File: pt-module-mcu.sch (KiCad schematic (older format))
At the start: 14 parts, among them SW8 SW_Push, SW9 SW_Push, U8 STM32F334R8Tx

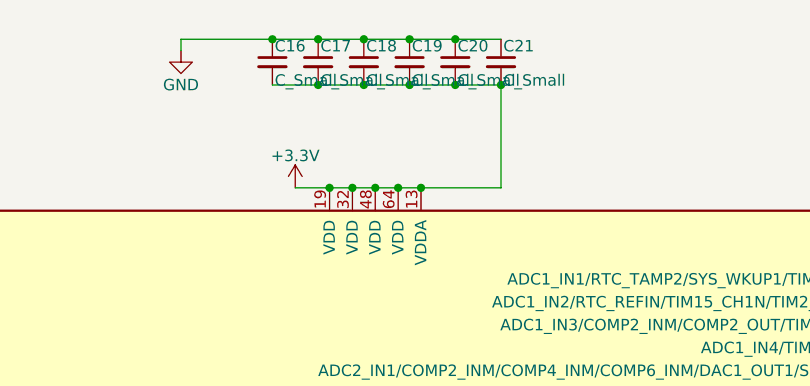
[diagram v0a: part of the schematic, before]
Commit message: Determined MCU power capacitor sizes, at last
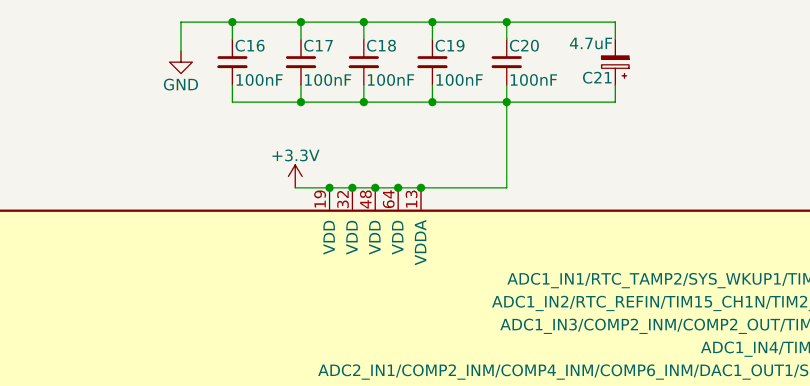
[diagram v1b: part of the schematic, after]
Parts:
- removed C21: C_Small, symbol C_Small
- added C21: 4.7uF, symbol CP_Small
- C16, C17, C18, C19, C20: value C_Small -> 100nF
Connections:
- net +3V3: now also C21.1
- net GND: now also C21.2
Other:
- moved on the sheet: C16, C17, C19, C20
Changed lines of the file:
@@
 $EndComp
 $Comp
-L GND #PWR079
+L GND #PWR74
 U 1 1 597EDE48
 P 1150 6800
-F 0 "#PWR079" H 1150 6550 50  0001 C CNN
+F 0 "#PWR74" H 1150 6550 50  0001 C CNN
 F 1 "GND" H 1150 6650 50  0000 C CNN
 F 2 "" H 1150 6800 50  0001 C CNN
@@
 $EndComp
 $Comp
-L GND #PWR080
+L GND #PWR77
 U 1 1 597EDE64
 P 1850 6800
-F 0 "#PWR080" H 1850 6550 50  0001 C CNN
+F 0 "#PWR77" H 1850 6550 50  0001 C CNN
 F 1 "GND" H 1850 6650 50  0000 C CNN
 F 2 "" H 1850 6800 50  0001 C CNN
@@
 $EndComp
 $Comp
-L GND #PWR081
+L GND #PWR75
 U 1 1 597EF838
 P 1750 1850
-F 0 "#PWR081" H 1750 1600 50  0001 C CNN
+F 0 "#PWR75" H 1750 1600 50  0001 C CNN
 F 1 "GND" H 1750 1700 50  0000 C CNN
 F 2 "" H 1750 1850 50  0001 C CNN
@@
 L C_Small C17
 U 1 1 597F1898
-P 6000 1100
-F 0 "C17" H 6010 1170 50  0000 L CNN
-F 1 "C_Small" H 6010 1020 50  0000 L CNN
-F 2 "" H 6000 1100 50  0001 C CNN
-F 3 "" H 6000 1100 50  0001 C CNN
-	1    6000 1100
-	1    0    0    -1
-$EndComp
-$Comp
-L C_Small C18
-U 1 1 597F1903
-P 6200 1100
-F 0 "C18" H 6210 1170 50  0000 L CNN
-F 1 "C_Small" H 6210 1020 50  0000 L CNN
-F 2 "" H 6200 1100 50  0001 C CNN
-F 3 "" H 6200 1100 50  0001 C CNN
-	1    6200 1100
+P 5925 1100
+F 0 "C17" H 5935 1170 50  0000 L CNN
+F 1 "100nF" H 5935 1020 50  0000 L CNN
+F 2 "" H 5925 1100 50  0001 C CNN
+F 3 "" H 5925 1100 50  0001 C CNN
+	1    5925 1100
 	1    0    0    -1
 $EndComp
@@
 L C_Small C19
 U 1 1 597F1997
-P 6400 1100
-F 0 "C19" H 6410 1170 50  0000 L CNN
-F 1 "C_Small" H 6410 1020 50  0000 L CNN
-F 2 "" H 6400 1100 50  0001 C CNN
-F 3 "" H 6400 1100 50  0001 C CNN
-	1    6400 1100
+P 6500 1100
+F 0 "C19" H 6510 1170 50  0000 L CNN
+F 1 "100nF" H 6510 1020 50  0000 L CNN
+F 2 "" H 6500 1100 50  0001 C CNN
+F 3 "" H 6500 1100 50  0001 C CNN
+	1    6500 1100
 	1    0    0    -1
 $EndComp
@@
 L C_Small C20
 U 1 1 597F19E6
-P 6600 1100
-F 0 "C20" H 6610 1170 50  0000 L CNN
-F 1 "C_Small" H 6610 1020 50  0000 L CNN
-F 2 "" H 6600 1100 50  0001 C CNN
-F 3 "" H 6600 1100 50  0001 C CNN
-	1    6600 1100
+P 6825 1100
+F 0 "C20" H 6835 1170 50  0000 L CNN
+F 1 "100nF" H 6835 1020 50  0000 L CNN
+F 2 "" H 6825 1100 50  0001 C CNN
+F 3 "" H 6825 1100 50  0001 C CNN
+	1    6825 1100
 	1    0    0    -1
 $EndComp
@@
 L C_Small C16
 U 1 1 597F1A58
-P 5800 1100
-F 0 "C16" H 5810 1170 50  0000 L CNN
-F 1 "C_Small" H 5810 1020 50  0000 L CNN
-F 2 "" H 5800 1100 50  0001 C CNN
-F 3 "" H 5800 1100 50  0001 C CNN
-	1    5800 1100
-	1    0    0    -1
-$EndComp
-$Comp
-L C_Small C21
-U 1 1 597F1AA1
-P 6800 1100
-F 0 "C21" H 6810 1170 50  0000 L CNN
-F 1 "C_Small" H 6810 1020 50  0000 L CNN
-F 2 "" H 6800 1100 50  0001 C CNN
-F 3 "" H 6800 1100 50  0001 C CNN
-	1    6800 1100
-	1    0    0    -1
-$EndComp
-$Comp
-L GND #PWR082
+P 5625 1100
+F 0 "C16" H 5635 1170 50  0000 L CNN
+F 1 "100nF" H 5635 1020 50  0000 L CNN
+F 2 "" H 5625 1100 50  0001 C CNN
+F 3 "" H 5625 1100 50  0001 C CNN
+	1    5625 1100
+	1    0    0    -1
+$EndComp
+$Comp
+L GND #PWR78
 U 1 1 597F238E
 P 5400 1050
-F 0 "#PWR082" H 5400 800 50  0001 C CNN
+F 0 "#PWR78" H 5400 800 50  0001 C CNN
 F 1 "GND" H 5400 900 50  0000 C CNN
 F 2 "" H 5400 1050 50  0001 C CNN
@@
 NoConn ~ 2550 2450
 $Comp
-L +3.3V #PWR083
+L +3.3V #PWR79
 U 1 1 5980C7A4
 P 5900 1650
-F 0 "#PWR083" H 5900 1500 50  0001 C CNN
+F 0 "#PWR79" H 5900 1500 50  0001 C CNN
 F 1 "+3.3V" H 5900 1790 50  0000 C CNN
 F 2 "" H 5900 1650 50  0001 C CNN
@@
 $EndComp
 $Comp
-L +3.3V #PWR084
+L +3.3V #PWR76
 U 1 1 5980CC21
 P 1750 2050
-F 0 "#PWR084" H 1750 1900 50  0001 C CNN
+F 0 "#PWR76" H 1750 1900 50  0001 C CNN
 F 1 "+3.3V" H 1750 2190 50  0000 C CNN
 F 2 "" H 1750 2050 50  0001 C CNN
@@
 Text HLabel 9950 5150 2    60   Output ~ 0
 UART3_de
-Connection ~ 6050 1650
-Wire Wire Line
-	1900 2050 1750 2050
-Wire Wire Line
-	1850 1850 1750 1850
-Connection ~ 2250 2050
-Wire Wire Line
-	2250 1850 2250 2050
-Wire Wire Line
-	2200 2050 2550 2050
-Connection ~ 1850 6400
-Connection ~ 1150 6400
-Wire Wire Line
-	1150 6700 1150 6800
-Wire Wire Line
-	1850 6700 1850 6800
-Wire Wire Line
-	1150 6250 1150 6500
-Wire Wire Line
-	1350 6400 1150 6400
-Wire Wire Line
-	1850 6250 1850 6500
-Wire Wire Line
-	1650 6400 1850 6400
-Wire Wire Line
-	5900 1650 6800 1650
-Connection ~ 6150 1650
-Connection ~ 6250 1650
-Connection ~ 6350 1650
-Wire Wire Line
-	6800 1650 6800 1200
-Connection ~ 6450 1650
-Wire Wire Line
-	6800 1200 5800 1200
-Connection ~ 6600 1200
-Connection ~ 6400 1200
-Connection ~ 6200 1200
-Connection ~ 6000 1200
-Wire Wire Line
-	5400 1000 6800 1000
-Connection ~ 6000 1000
-Connection ~ 6600 1000
-Connection ~ 6200 1000
-Connection ~ 6400 1000
-Connection ~ 5800 1000
-Connection ~ 6800 1200
 Text HLabel 9950 4350 2    60   Input ~ 0
 UART1_TX
@@
 $EndComp
 $Comp
-L GND #PWR085
+L GND #PWR73
 U 1 1 598A8EB8
 P 950 2250
-F 0 "#PWR085" H 950 2000 50  0001 C CNN
+F 0 "#PWR73" H 950 2000 50  0001 C CNN
 F 1 "GND" H 950 2100 50  0000 C CNN
 F 2 "" H 950 2250 50  0001 C CNN
@@
 $EndComp
 $Comp
-L +3.3V #PWR086
+L +3.3V #PWR72
 U 1 1 598A8EC4
 P 950 2050
-F 0 "#PWR086" H 950 1900 50  0001 C CNN
+F 0 "#PWR72" H 950 1900 50  0001 C CNN
 F 1 "+3.3V" H 950 2190 50  0000 C CNN
 F 2 "" H 950 2050 50  0001 C CNN
@@
 	0    -1   -1   0
 $EndComp
-Wire Wire Line
-	1100 2250 950  2250
-Wire Wire Line
-	1050 2050 950  2050
-Connection ~ 1450 2250
-Wire Wire Line
-	1450 2050 1450 2250
-Wire Wire Line
-	1400 2250 2550 2250
-Wire Wire Line
-	6050 5650 6050 5700
-Wire Wire Line
-	6050 5700 6450 5700
-Wire Wire Line
-	6450 5700 6450 5650
-Wire Wire Line
-	6350 5650 6350 5700
-Connection ~ 6350 5700
-Wire Wire Line
-	6250 5650 6250 5800
-Connection ~ 6250 5700
-Wire Wire Line
-	6150 5650 6150 5700
-Connection ~ 6150 5700
-$Comp
-L GND #PWR087
+$Comp
+L GND #PWR80
 U 1 1 598A971D
 P 6250 5800
-F 0 "#PWR087" H 6250 5550 50  0001 C CNN
+F 0 "#PWR80" H 6250 5550 50  0001 C CNN
 F 1 "GND" H 6250 5650 50  0000 C CNN
 F 2 "" H 6250 5800 50  0001 C CNN
@@
 	1    0    0    -1
 $EndComp
-Wire Wire Line
-	5400 1000 5400 1050
 Text HLabel 2550 3750 0    60   Input ~ 0
 prb_btn_1_pwr
@@
 NoConn ~ 9950 4950
 NoConn ~ 9950 5050
+$Comp
+L CP_Small C21
+U 1 1 5994BDA8
+P 7300 1100
+F 0 "C21" H 7310 1170 50  0000 L CNN
+F 1 "4.7uF" H 7310 1020 50  0000 L CNN
+F 2 "" H 7300 1100 50  0001 C CNN
+F 3 "" H 7300 1100 50  0001 C CNN
+	1    7300 1100
+	-1   0    0    1
+$EndComp
+$Comp
+L C_Small C18
+U 1 1 597F1903
+P 6200 1100
+F 0 "C18" H 6210 1170 50  0000 L CNN
+F 1 "100nF" H 6210 1020 50  0000 L CNN
+F 2 "" H 6200 1100 50  0001 C CNN
+F 3 "" H 6200 1100 50  0001 C CNN
+	1    6200 1100
+	1    0    0    -1
+$EndComp
+Connection ~ 6050 1650
+Wire Wire Line
+	1900 2050 1750 2050
+Wire Wire Line
+	1850 1850 1750 1850
+Connection ~ 2250 2050
+Wire Wire Line
+	2250 1850 2250 2050
+Wire Wire Line
+	2200 2050 2550 2050
+Connection ~ 1850 6400
+Connection ~ 1150 6400
+Wire Wire Line
+	1150 6700 1150 6800
+Wire Wire Line
+	1850 6700 1850 6800
+Wire Wire Line
+	1150 6250 1150 6500
+Wire Wire Line
+	1350 6400 1150 6400
+Wire Wire Line
+	1850 6250 1850 6500
+Wire Wire Line
+	1650 6400 1850 6400
+Wire Wire Line
+	6825 1650 5900 1650
+Connection ~ 6150 1650
+Connection ~ 6250 1650
+Connection ~ 6350 1650
+Connection ~ 6450 1650
+Wire Wire Line
+	1100 2250 950  2250
+Wire Wire Line
+	1050 2050 950  2050
+Connection ~ 1450 2250
+Wire Wire Line
+	1450 2050 1450 2250
+Wire Wire Line
+	1400 2250 2550 2250
+Wire Wire Line
+	6050 5650 6050 5700
+Wire Wire Line
+	6050 5700 6450 5700
+Wire Wire Line
+	6450 5700 6450 5650
+Wire Wire Line
+	6350 5650 6350 5700
+Connection ~ 6350 5700
+Wire Wire Line
+	6250 5650 6250 5800
+Connection ~ 6250 5700
+Wire Wire Line
+	6150 5650 6150 5700
+Connection ~ 6150 5700
+Wire Wire Line
+	5400 925  5400 1050
+Wire Wire Line
+	5625 1000 5625 925
+Wire Wire Line
+	5400 925  7300 925
+Wire Wire Line
+	7300 925  7300 1000
+Wire Wire Line
+	6825 1000 6825 925
+Connection ~ 6825 925
+Wire Wire Line
+	6500 1000 6500 925
+Connection ~ 6500 925
+Wire Wire Line
+	6200 1000 6200 925
+Connection ~ 6200 925
+Wire Wire Line
+	5925 1000 5925 925
+Connection ~ 5925 925
+Connection ~ 5625 925
+Wire Wire Line
+	7300 1200 7300 1275
+Wire Wire Line
+	7300 1275 5625 1275
+Wire Wire Line
+	5625 1275 5625 1200
+Wire Wire Line
+	5925 1200 5925 1275
+Connection ~ 5925 1275
+Wire Wire Line
+	6200 1200 6200 1275
+Connection ~ 6200 1275
+Wire Wire Line
+	6500 1200 6500 1275
+Connection ~ 6500 1275
+Wire Wire Line
+	6825 1200 6825 1650
+Connection ~ 6825 1275
 $EndSCHEMATC

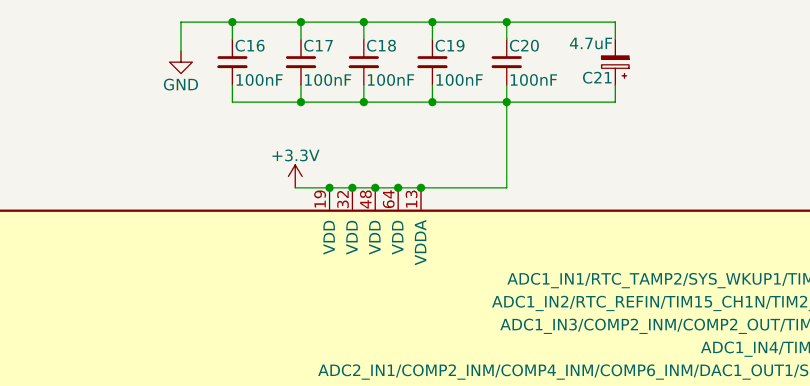
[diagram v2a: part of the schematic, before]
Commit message: add all the rest of the footprints
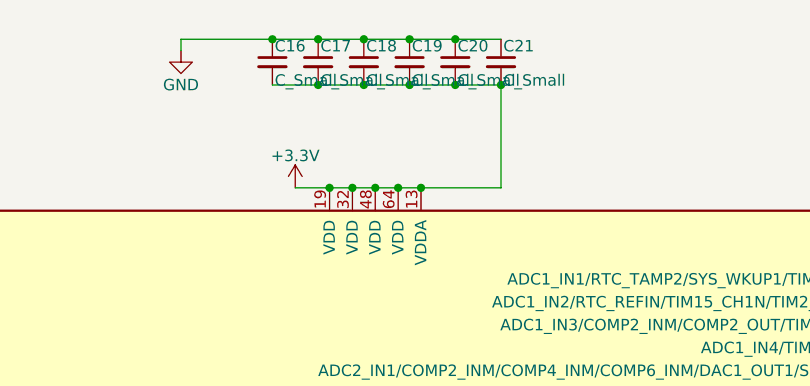
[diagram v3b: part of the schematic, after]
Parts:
- removed C21: 4.7uF, symbol CP_Small
- added C21: C_Small, Capacitors_SMD:C_1206_HandSoldering, symbol C_Small
- 16Mhz1: footprint (none) -> .pretty:HC49_Crystal
- C14, C15: footprint (none) -> Capacitors_SMD:C_1206_HandSoldering
- C16, C17, C18, C19, C20: value 100nF -> C_Small; footprint (none) -> Capacitors_SMD:C_1206_HandSoldering
- R25, R26: footprint (none) -> Resistors_SMD:R_1206_HandSoldering
- SW8, SW9: footprint (none) -> Connectors_Hirose:Hirose_DF13C-02P-1.25V_02x1.25mm_Straight
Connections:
- net +3V3: now also C21.2
- net GND: now also C21.1
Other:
- moved on the sheet: C16, C17, C19, C20
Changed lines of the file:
@@
 F 0 "16Mhz1" H 1500 6550 50  0000 C CNN
 F 1 "Crystal" H 1500 6250 50  0000 C CNN
-F 2 "" H 1500 6400 50  0001 C CNN
+F 2 ".pretty:HC49_Crystal" H 1500 6400 50  0001 C CNN
 F 3 "" H 1500 6400 50  0001 C CNN
 	1    1500 6400
@@
 F 0 "C14" H 1160 6670 50  0000 L CNN
 F 1 "27pF" H 1160 6520 50  0000 L CNN
-F 2 "" H 1150 6600 50  0001 C CNN
+F 2 "Capacitors_SMD:C_1206_HandSoldering" H 1150 6600 50  0001 C CNN
 F 3 "" H 1150 6600 50  0001 C CNN
 	1    1150 6600
@@
 F 0 "C15" H 1860 6670 50  0000 L CNN
 F 1 "27pF" H 1860 6520 50  0000 L CNN
-F 2 "" H 1850 6600 50  0001 C CNN
+F 2 "Capacitors_SMD:C_1206_HandSoldering" H 1850 6600 50  0001 C CNN
 F 3 "" H 1850 6600 50  0001 C CNN
 	1    1850 6600
@@
 F 0 "R26" V 2130 2050 50  0000 C CNN
 F 1 "10k" V 2050 2050 50  0000 C CNN
-F 2 "" V 1980 2050 50  0001 C CNN
+F 2 "Resistors_SMD:R_1206_HandSoldering" V 1980 2050 50  0001 C CNN
 F 3 "" H 2050 2050 50  0001 C CNN
 	1    2050 2050
@@
 F 0 "SW9" H 2100 1950 50  0000 L CNN
 F 1 "SW_Push" H 2050 1790 50  0000 C CNN
-F 2 "" H 2050 2050 50  0001 C CNN
+F 2 "Connectors_Hirose:Hirose_DF13C-02P-1.25V_02x1.25mm_Straight" H 2050 2050 50  0001 C CNN
 F 3 "" H 2050 2050 50  0001 C CNN
 	1    2050 1850
@@
 L C_Small C17
 U 1 1 597F1898
-P 5925 1100
-F 0 "C17" H 5935 1170 50  0000 L CNN
-F 1 "100nF" H 5935 1020 50  0000 L CNN
-F 2 "" H 5925 1100 50  0001 C CNN
-F 3 "" H 5925 1100 50  0001 C CNN
-	1    5925 1100
+P 6000 1100
+F 0 "C17" H 6010 1170 50  0000 L CNN
+F 1 "C_Small" H 6010 1020 50  0000 L CNN
+F 2 "Capacitors_SMD:C_1206_HandSoldering" H 6000 1100 50  0001 C CNN
+F 3 "" H 6000 1100 50  0001 C CNN
+	1    6000 1100
+	1    0    0    -1
+$EndComp
+$Comp
+L C_Small C18
+U 1 1 597F1903
+P 6200 1100
+F 0 "C18" H 6210 1170 50  0000 L CNN
+F 1 "C_Small" H 6210 1020 50  0000 L CNN
+F 2 "Capacitors_SMD:C_1206_HandSoldering" H 6200 1100 50  0001 C CNN
+F 3 "" H 6200 1100 50  0001 C CNN
+	1    6200 1100
 	1    0    0    -1
 $EndComp
@@
 L C_Small C19
 U 1 1 597F1997
-P 6500 1100
-F 0 "C19" H 6510 1170 50  0000 L CNN
-F 1 "100nF" H 6510 1020 50  0000 L CNN
-F 2 "" H 6500 1100 50  0001 C CNN
-F 3 "" H 6500 1100 50  0001 C CNN
-	1    6500 1100
+P 6400 1100
+F 0 "C19" H 6410 1170 50  0000 L CNN
+F 1 "C_Small" H 6410 1020 50  0000 L CNN
+F 2 "Capacitors_SMD:C_1206_HandSoldering" H 6400 1100 50  0001 C CNN
+F 3 "" H 6400 1100 50  0001 C CNN
+	1    6400 1100
 	1    0    0    -1
 $EndComp
@@
 L C_Small C20
 U 1 1 597F19E6
-P 6825 1100
-F 0 "C20" H 6835 1170 50  0000 L CNN
-F 1 "100nF" H 6835 1020 50  0000 L CNN
-F 2 "" H 6825 1100 50  0001 C CNN
-F 3 "" H 6825 1100 50  0001 C CNN
-	1    6825 1100
+P 6600 1100
+F 0 "C20" H 6610 1170 50  0000 L CNN
+F 1 "C_Small" H 6610 1020 50  0000 L CNN
+F 2 "Capacitors_SMD:C_1206_HandSoldering" H 6600 1100 50  0001 C CNN
+F 3 "" H 6600 1100 50  0001 C CNN
+	1    6600 1100
 	1    0    0    -1
 $EndComp
@@
 L C_Small C16
 U 1 1 597F1A58
-P 5625 1100
-F 0 "C16" H 5635 1170 50  0000 L CNN
-F 1 "100nF" H 5635 1020 50  0000 L CNN
-F 2 "" H 5625 1100 50  0001 C CNN
-F 3 "" H 5625 1100 50  0001 C CNN
-	1    5625 1100
+P 5800 1100
+F 0 "C16" H 5810 1170 50  0000 L CNN
+F 1 "C_Small" H 5810 1020 50  0000 L CNN
+F 2 "Capacitors_SMD:C_1206_HandSoldering" H 5800 1100 50  0001 C CNN
+F 3 "" H 5800 1100 50  0001 C CNN
+	1    5800 1100
+	1    0    0    -1
+$EndComp
+$Comp
+L C_Small C21
+U 1 1 597F1AA1
+P 6800 1100
+F 0 "C21" H 6810 1170 50  0000 L CNN
+F 1 "C_Small" H 6810 1020 50  0000 L CNN
+F 2 "Capacitors_SMD:C_1206_HandSoldering" H 6800 1100 50  0001 C CNN
+F 3 "" H 6800 1100 50  0001 C CNN
+	1    6800 1100
 	1    0    0    -1
 $EndComp
@@
 Text HLabel 9950 5150 2    60   Output ~ 0
 UART3_de
+Connection ~ 6050 1650
+Wire Wire Line
+	1900 2050 1750 2050
+Wire Wire Line
+	1850 1850 1750 1850
+Connection ~ 2250 2050
+Wire Wire Line
+	2250 1850 2250 2050
+Wire Wire Line
+	2200 2050 2550 2050
+Connection ~ 1850 6400
+Connection ~ 1150 6400
+Wire Wire Line
+	1150 6700 1150 6800
+Wire Wire Line
+	1850 6700 1850 6800
+Wire Wire Line
+	1150 6250 1150 6500
+Wire Wire Line
+	1350 6400 1150 6400
+Wire Wire Line
+	1850 6250 1850 6500
+Wire Wire Line
+	1650 6400 1850 6400
+Wire Wire Line
+	5900 1650 6800 1650
+Connection ~ 6150 1650
+Connection ~ 6250 1650
+Connection ~ 6350 1650
+Wire Wire Line
+	6800 1650 6800 1200
+Connection ~ 6450 1650
+Wire Wire Line
+	6800 1200 5800 1200
+Connection ~ 6600 1200
+Connection ~ 6400 1200
+Connection ~ 6200 1200
+Connection ~ 6000 1200
+Wire Wire Line
+	5400 1000 6800 1000
+Connection ~ 6000 1000
+Connection ~ 6600 1000
+Connection ~ 6200 1000
+Connection ~ 6400 1000
+Connection ~ 5800 1000
+Connection ~ 6800 1200
 Text HLabel 9950 4350 2    60   Input ~ 0
 UART1_TX
@@
 F 0 "R25" V 1330 2250 50  0000 C CNN
 F 1 "10k" V 1250 2250 50  0000 C CNN
-F 2 "" V 1180 2250 50  0001 C CNN
+F 2 "Resistors_SMD:R_1206_HandSoldering" V 1180 2250 50  0001 C CNN
 F 3 "" H 1250 2250 50  0001 C CNN
 	1    1250 2250
@@
 F 0 "SW8" H 1300 2150 50  0000 L CNN
 F 1 "SW_Push" H 1250 1990 50  0000 C CNN
-F 2 "" H 1250 2250 50  0001 C CNN
+F 2 "Connectors_Hirose:Hirose_DF13C-02P-1.25V_02x1.25mm_Straight" H 1250 2250 50  0001 C CNN
 F 3 "" H 1250 2250 50  0001 C CNN
 	1    1250 2050
@@
 	0    -1   -1   0
 $EndComp
+Wire Wire Line
+	1100 2250 950  2250
+Wire Wire Line
+	1050 2050 950  2050
+Connection ~ 1450 2250
+Wire Wire Line
+	1450 2050 1450 2250
+Wire Wire Line
+	1400 2250 2550 2250
+Wire Wire Line
+	6050 5650 6050 5700
+Wire Wire Line
+	6050 5700 6450 5700
+Wire Wire Line
+	6450 5700 6450 5650
+Wire Wire Line
+	6350 5650 6350 5700
+Connection ~ 6350 5700
+Wire Wire Line
+	6250 5650 6250 5800
+Connection ~ 6250 5700
+Wire Wire Line
+	6150 5650 6150 5700
+Connection ~ 6150 5700
 $Comp
 L GND #PWR087
@@
 	1    0    0    -1
 $EndComp
+Wire Wire Line
+	5400 1000 5400 1050
 Text HLabel 2550 3750 0    60   Input ~ 0
 prb_btn_1_pwr
@@
 NoConn ~ 9950 4950
 NoConn ~ 9950 5050
-$Comp
-L CP_Small C21
-U 1 1 5994BDA8
-P 7300 1100
-F 0 "C21" H 7310 1170 50  0000 L CNN
-F 1 "4.7uF" H 7310 1020 50  0000 L CNN
-F 2 "" H 7300 1100 50  0001 C CNN
-F 3 "" H 7300 1100 50  0001 C CNN
-	1    7300 1100
-	-1   0    0    1
-$EndComp
-$Comp
-L C_Small C18
-U 1 1 597F1903
-P 6200 1100
-F 0 "C18" H 6210 1170 50  0000 L CNN
-F 1 "100nF" H 6210 1020 50  0000 L CNN
-F 2 "" H 6200 1100 50  0001 C CNN
-F 3 "" H 6200 1100 50  0001 C CNN
-	1    6200 1100
-	1    0    0    -1
-$EndComp
-Connection ~ 6050 1650
-Wire Wire Line
-	1900 2050 1750 2050
-Wire Wire Line
-	1850 1850 1750 1850
-Connection ~ 2250 2050
-Wire Wire Line
-	2250 1850 2250 2050
-Wire Wire Line
-	2200 2050 2550 2050
-Connection ~ 1850 6400
-Connection ~ 1150 6400
-Wire Wire Line
-	1150 6700 1150 6800
-Wire Wire Line
-	1850 6700 1850 6800
-Wire Wire Line
-	1150 6250 1150 6500
-Wire Wire Line
-	1350 6400 1150 6400
-Wire Wire Line
-	1850 6250 1850 6500
-Wire Wire Line
-	1650 6400 1850 6400
-Wire Wire Line
-	6825 1650 5900 1650
-Connection ~ 6150 1650
-Connection ~ 6250 1650
-Connection ~ 6350 1650
-Connection ~ 6450 1650
-Wire Wire Line
-	1100 2250 950  2250
-Wire Wire Line
-	1050 2050 950  2050
-Connection ~ 1450 2250
-Wire Wire Line
-	1450 2050 1450 2250
-Wire Wire Line
-	1400 2250 2550 2250
-Wire Wire Line
-	6050 5650 6050 5700
-Wire Wire Line
-	6050 5700 6450 5700
-Wire Wire Line
-	6450 5700 6450 5650
-Wire Wire Line
-	6350 5650 6350 5700
-Connection ~ 6350 5700
-Wire Wire Line
-	6250 5650 6250 5800
-Connection ~ 6250 5700
-Wire Wire Line
-	6150 5650 6150 5700
-Connection ~ 6150 5700
-Wire Wire Line
-	5400 925  5400 1050
-Wire Wire Line
-	5625 1000 5625 925
-Wire Wire Line
-	5400 925  7300 925
-Wire Wire Line
-	7300 925  7300 1000
-Wire Wire Line
-	6825 1000 6825 925
-Connection ~ 6825 925
-Wire Wire Line
-	6500 1000 6500 925
-Connection ~ 6500 925
-Wire Wire Line
-	6200 1000 6200 925
-Connection ~ 6200 925
-Wire Wire Line
-	5925 1000 5925 925
-Connection ~ 5925 925
-Connection ~ 5625 925
-Wire Wire Line
-	7300 1200 7300 1275
-Wire Wire Line
-	7300 1275 5625 1275
-Wire Wire Line
-	5625 1275 5625 1200
-Wire Wire Line
-	5925 1200 5925 1275
-Connection ~ 5925 1275
-Wire Wire Line
-	6200 1200 6200 1275
-Connection ~ 6200 1275
-Wire Wire Line
-	6500 1200 6500 1275
-Connection ~ 6500 1275
-Wire Wire Line
-	6825 1200 6825 1650
-Connection ~ 6825 1275
 $EndSCHEMATC

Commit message: start the pcb
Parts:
- U8: footprint LQFP64 -> Housings_QFP:LQFP-64_10x10mm_Pitch0.5mm
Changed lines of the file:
@@
 F 0 "U8" H 2650 5575 50  0000 L BNN
 F 1 "STM32F334R8Tx" H 9850 5575 50  0000 R BNN
-F 2 "LQFP64" H 9850 5525 50  0001 R TNN
+F 2 "Housings_QFP:LQFP-64_10x10mm_Pitch0.5mm" H 9850 5525 50  0001 R TNN
 F 3 "" H 6250 3650 50  0001 C CNN
 	1    6250 3650
